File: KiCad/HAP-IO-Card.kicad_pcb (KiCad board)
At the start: 2 copper layers, 110 x 72 mm, 369 parts, among them CON601 AVR-JTAG-10, J201 TE_Connectivity_1-282834-0, J202 TE_Connectivity_282834-6, J203 GS3, J204 GS3, J205 GS3, J206 GS3, J207 GS3, J208 GS3, J209 GS3, J210 GS3, J211 TE_Connectivity_282834-6, J212 TE_Connectivity_1-282834-0, J401 TE_Connectivity_1-282834-0, J402 TE_Connectivity_282834-6, J501 TE_Connectivity_282834-3, J502 CONN_01X03_FEMALE, J601 ISP0, J602 ISP1, J603 CONN_01X02, J604 CONN_01X02, J605 CONN_01X02, J606 CONN_01X02, J607 CONN_01X03, J608 CONN_01X03, J701 5V_I/O_2, J702 5V_I/O_1, J703 NEO1, J704 NEO2, J705 NEO3, J706 NEO4, J707 CONN_01X03, Q201 ZXTN25050DFHTA, Q202 ZXTN25050DFHTA, Q203 ZXTN25050DFHTA, Q204 ZXTN25050DFHTA, Q205 ZXTN25050DFHTA, Q206 ZXTN25050DFHTA, Q207 ZXTN25050DFHTA, Q208 ZXTN25050DFHTA, U201 LTV-354T, U202 LTV-354T, U203 LTV-354T, U204 LTV-354T, U205 LTV-354T, U206 LTV-354T, U207 LTV-354T, U208 LTV-354T, U209 MCP23017, U401 ADS1115IDGST, U402 ADS1115IDGST, U501 LM1086-5V, U502 LM1086-3.3V, U701 TXB0102DCT

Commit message: Groudplanes
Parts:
- removed the REF** at (38.4, 79.5)
- removed the REF** at (38.4, 76.9)
- removed the REF** at (38.4, 74.4)
- removed the REF** at (38.4, 71.8)
- removed the REF** at (38.4, 69.3)
- removed the REF** at (38.4, 66.8)
- removed the REF** at (38.4, 64.2)
- removed the REF** at (38.4, 61.7)
- removed the REF** at (38.4, 59.1)
- removed the REF** at (38.4, 56.6)
- removed the REF** at (38.4, 54.1)
- removed the REF** at (99.3, 61.6)
- removed the REF** at (97.5, 63.3)
- added REF**: StichingVia, StichingVIA:StichingVia, F.Cu at (77.0, 71.9)
- added REF**: StichingVia, StichingVIA:StichingVia, F.Cu at (93.0, 41.1)
- added REF**: StichingVia, StichingVIA:StichingVia, F.Cu at (48.0, 81.5)
- added REF**: StichingVia, StichingVIA:StichingVia, F.Cu at (49.5, 82.8)
- added REF**: StichingVia, StichingVIA:StichingVia, F.Cu at (52.3, 76.7)
- added REF**: StichingVia, StichingVIA:StichingVia, F.Cu at (54.6, 76.7)
- added REF**: StichingVia, StichingVIA:StichingVia, F.Cu at (54.6, 74.7)
- added REF**: StichingVia, StichingVIA:StichingVia, F.Cu at (93.2, 71.6)
- added REF**: StichingVia, StichingVIA:StichingVia, F.Cu at (55.9, 49.5)
- added REF**: StichingVia, StichingVIA:StichingVia, F.Cu at (53.3, 49.5)
- added REF**: StichingVia, StichingVIA:StichingVia, F.Cu at (50.8, 49.5)
- added REF**: StichingVia, StichingVIA:StichingVia, F.Cu at (78.7, 71.9)
- added REF**: StichingVia, StichingVIA:StichingVia, F.Cu at (48.2, 49.5)
- added REF**: StichingVia, StichingVIA:StichingVia, F.Cu at (45.7, 49.5)
- added REF**: StichingVia, StichingVIA:StichingVia, F.Cu at (73.5, 64.8)
- added REF**: StichingVia, StichingVIA:StichingVia, F.Cu at (73.5, 62.2)
- added REF**: StichingVia, StichingVIA:StichingVia, F.Cu at (86.1, 65.4)
- added REF**: StichingVia, StichingVIA:StichingVia, F.Cu at (92.3, 60.3)
- added REF**: StichingVia, StichingVIA:StichingVia, F.Cu at (92.3, 62.9)
- added REF**: StichingVia, StichingVIA:StichingVia, F.Cu at (87.1, 67.7)
- added REF**: StichingVia, StichingVIA:StichingVia, F.Cu at (88.7, 60.4)
- added REF**: StichingVia, StichingVIA:StichingVia, F.Cu at (88.7, 65.4)
- added REF**: StichingVia, StichingVIA:StichingVia, F.Cu at (81.0, 71.9)
- added REF**: StichingVia, StichingVIA:StichingVia, F.Cu at (88.7, 62.9)
- added REF**: StichingVia, StichingVIA:StichingVia, F.Cu at (62.6, 70.0)
- added REF**: StichingVia, StichingVIA:StichingVia, F.Cu at (62.6, 62.4)
- added REF**: StichingVia, StichingVIA:StichingVia, F.Cu at (62.6, 67.5)
- added REF**: StichingVia, StichingVIA:StichingVia, F.Cu at (62.6, 64.9)
- added REF**: StichingVia, StichingVIA:StichingVia, F.Cu at (59.0, 62.4)
- added REF**: StichingVia, StichingVIA:StichingVia, F.Cu at (59.0, 70.0)
- added REF**: StichingVia, StichingVIA:StichingVia, F.Cu at (59.0, 64.9)
- added REF**: StichingVia, StichingVIA:StichingVia, F.Cu at (59.0, 67.5)
- added REF**: StichingVia, StichingVIA:StichingVia, F.Cu at (50.2, 64.9)
- added REF**: StichingVia, StichingVIA:StichingVia, F.Cu at (83.8, 71.9)
- added REF**: StichingVia, StichingVIA:StichingVia, F.Cu at (50.2, 67.4)
- added REF**: StichingVia, StichingVIA:StichingVia, F.Cu at (50.2, 70.0)
- added REF**: StichingVia, StichingVIA:StichingVia, F.Cu at (50.2, 62.4)
- added REF**: StichingVia, StichingVIA:StichingVia, F.Cu at (53.1, 62.4)
- added REF**: StichingVia, StichingVIA:StichingVia, F.Cu at (53.1, 70.0)
- added REF**: StichingVia, StichingVIA:StichingVia, F.Cu at (53.1, 67.4)
- added REF**: StichingVia, StichingVIA:StichingVia, F.Cu at (53.1, 64.9)
- added REF**: StichingVia, StichingVIA:StichingVia, F.Cu at (46.6, 70.0)
- added REF**: StichingVia, StichingVIA:StichingVia, F.Cu at (46.6, 67.4)
- added REF**: StichingVia, StichingVIA:StichingVia, F.Cu at (46.6, 64.9)
- added REF**: StichingVia, StichingVIA:StichingVia, F.Cu at (88.6, 82.3)
- added REF**: StichingVia, StichingVIA:StichingVia, F.Cu at (46.6, 62.4)
- added REF**: StichingVia, StichingVIA:StichingVia, F.Cu at (87.1, 83.3)
- added REF**: StichingVia, StichingVIA:StichingVia, F.Cu at (87.1, 81.8)
- added REF**: StichingVia, StichingVIA:StichingVia, F.Cu at (49.5, 81.5)
- added REF**: StichingVia, StichingVIA:StichingVia, F.Cu at (99.6, 42.7)
- moved REF** 0.88 mm to (99.8, 65.3)
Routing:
- net DIGITAL_INTA: track 63.5 -> 62.9 mm
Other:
- board text added: "1"
- board text added: "5VI/O1"
- board text added: "5VI/O2"
- board text added: "I38"
- board text added: "I39"
- board text added: "IO0/ Btn"
- board text added: "IO5/ LED"
- board text added: "JTAG"

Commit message: More groundplane
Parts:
- added REF**: StichingVia, StichingVIA:StichingVia, F.Cu at (117.1, 63.2)
- added REF**: StichingVia, StichingVIA:StichingVia, F.Cu at (119.1, 61.2)
- added REF**: StichingVia, StichingVIA:StichingVia, F.Cu at (126.2, 45.5)
- added REF**: StichingVia, StichingVIA:StichingVia, F.Cu at (126.2, 61.2)
- added REF**: StichingVia, StichingVIA:StichingVia, F.Cu at (126.2, 71.4)
- added REF**: StichingVia, StichingVIA:StichingVia, F.Cu at (132.1, 71.4)
- added REF**: StichingVia, StichingVIA:StichingVia, F.Cu at (121.7, 71.6)
- added REF**: StichingVia, StichingVIA:StichingVia, F.Cu at (118.1, 69.1)
- added REF**: StichingVia, StichingVIA:StichingVia, F.Cu at (114.3, 67.1)
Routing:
- net Earth: track 95.2 -> 83.7 mm, vias 16 -> 15
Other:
- net class 12V: trace_width 0.4 -> 1.27
- net class 3V3: trace_width 0.3 -> 0.76
- net class 5V: trace_width 0.3 -> 0.76
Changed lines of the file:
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@@
 (kicad_pcb (version 20170123) (host pcbnew "(2017-05-31 revision c0bb8a30c)-makepkg")
   (general
-    (links 649)
+    (links 660)
     (no_connects 0)
     (area 34.499762 15.011666 148.383572 90.7625)
     (thickness 1.6)
     (drawings 198)
-    (tracks 1824)
+    (tracks 1818)
     (zones 0)
-    (modules 406)
+    (modules 415)
     (nets 162)
   )
@@
   (net_class 12V ""
     (clearance 0.3)
-    (trace_width 0.4)
+    (trace_width 1.27)
     (via_dia 0.6)
     (via_drill 0.4)
@@
   (net_class 3V3 ""
     (clearance 0.2)
-    (trace_width 0.3)
+    (trace_width 0.76)
     (via_dia 0.6)
     (via_drill 0.4)
@@
   (net_class 5V ""
     (clearance 0.2)
-    (trace_width 0.3)
+    (trace_width 0.76)
     (via_dia 0.6)
     (via_drill 0.4)
@@
   )
   (module StichingVIA:StichingVia locked (layer F.Cu)
+    (at 117.094 63.246)
+    (fp_text reference REF** (at -0.65 0.03) (layer F.SilkS) hide
+      (effects (font (size 0.127 0.127) (thickness 0.03175)))
+    )
+    (fp_text value StichingVia (at -0.86 0.14) (layer F.Fab) hide
+      (effects (font (size 0.127 0.127) (thickness 0.03175)))
+    )
+    (fp_circle (center 0 0) (end 0.22 0.12) (layer F.CrtYd) (width 0.1))
+    (fp_circle (center 0 0) (end 0.25 0) (layer B.CrtYd) (width 0.1))
+    (pad 1 thru_hole circle (at 0 0) (size 0.6 0.6) (drill 0.3) (layers *.Cu)
+      (net 94 Earth) (zone_connect 2))
+  )
+  (module StichingVIA:StichingVia locked (layer F.Cu)
+    (at 119.126 61.214)
+    (fp_text reference REF** (at -0.65 0.03) (layer F.SilkS) hide
+      (effects (font (size 0.127 0.127) (thickness 0.03175)))
+    )
+    (fp_text value StichingVia (at -0.86 0.14) (layer F.Fab) hide
+      (effects (font (size 0.127 0.127) (thickness 0.03175)))
+    )
+    (fp_circle (center 0 0) (end 0.25 0) (layer B.CrtYd) (width 0.1))
+    (fp_circle (center 0 0) (end 0.22 0.12) (layer F.CrtYd) (width 0.1))
+    (pad 1 thru_hole circle (at 0 0) (size 0.6 0.6) (drill 0.3) (layers *.Cu)
+      (net 94 Earth) (zone_connect 2))
+  )
+  (module StichingVIA:StichingVia locked (layer F.Cu)
+    (at 126.238 45.466)
+    (fp_text reference REF** (at -0.65 0.03) (layer F.SilkS) hide
+      (effects (font (size 0.127 0.127) (thickness 0.03175)))
+    )
+    (fp_text value StichingVia (at -0.86 0.14) (layer F.Fab) hide
+      (effects (font (size 0.127 0.127) (thickness 0.03175)))
+    )
+    (fp_circle (center 0 0) (end 0.25 0) (layer B.CrtYd) (width 0.1))
+    (fp_circle (center 0 0) (end 0.22 0.12) (layer F.CrtYd) (width 0.1))
+    (pad 1 thru_hole circle (at 0 0) (size 0.6 0.6) (drill 0.3) (layers *.Cu)
+      (net 94 Earth) (zone_connect 2))
+  )
+  (module StichingVIA:StichingVia locked (layer F.Cu)
+    (at 126.238 61.214)
+    (fp_text reference REF** (at -0.65 0.03) (layer F.SilkS) hide
+      (effects (font (size 0.127 0.127) (thickness 0.03175)))
+    )
+    (fp_text value StichingVia (at -0.86 0.14) (layer F.Fab) hide
+      (effects (font (size 0.127 0.127) (thickness 0.03175)))
+    )
+    (fp_circle (center 0 0) (end 0.22 0.12) (layer F.CrtYd) (width 0.1))
+    (fp_circle (center 0 0) (end 0.25 0) (layer B.CrtYd) (width 0.1))
+    (pad 1 thru_hole circle (at 0 0) (size 0.6 0.6) (drill 0.3) (layers *.Cu)
+      (net 94 Earth) (zone_connect 2))
+  )
+  (module StichingVIA:StichingVia locked (layer F.Cu)
+    (at 126.238 71.374)
+    (fp_text reference REF** (at -0.65 0.03) (layer F.SilkS) hide
+      (effects (font (size 0.127 0.127) (thickness 0.03175)))
+    )
+    (fp_text value StichingVia (at -0.86 0.14) (layer F.Fab) hide
+      (effects (font (size 0.127 0.127) (thickness 0.03175)))
+    )
+    (fp_circle (center 0 0) (end 0.25 0) (layer B.CrtYd) (width 0.1))
+    (fp_circle (center 0 0) (end 0.22 0.12) (layer F.CrtYd) (width 0.1))
+    (pad 1 thru_hole circle (at 0 0) (size 0.6 0.6) (drill 0.3) (layers *.Cu)
+      (net 94 Earth) (zone_connect 2))
+  )
+  (module StichingVIA:StichingVia locked (layer F.Cu)
+    (at 132.08 71.374)
+    (fp_text reference REF** (at -0.65 0.03) (layer F.SilkS) hide
+      (effects (font (size 0.127 0.127) (thickness 0.03175)))
+    )
+    (fp_text value StichingVia (at -0.86 0.14) (layer F.Fab) hide
+      (effects (font (size 0.127 0.127) (thickness 0.03175)))
+    )
+    (fp_circle (center 0 0) (end 0.25 0) (layer B.CrtYd) (width 0.1))
+    (fp_circle (center 0 0) (end 0.22 0.12) (layer F.CrtYd) (width 0.1))
+    (pad 1 thru_hole circle (at 0 0) (size 0.6 0.6) (drill 0.3) (layers *.Cu)
+      (net 94 Earth) (zone_connect 2))
+  )
+  (module StichingVIA:StichingVia locked (layer F.Cu)
+    (at 121.666 71.628)
+    (fp_text reference REF** (at -0.65 0.03) (layer F.SilkS) hide
+      (effects (font (size 0.127 0.127) (thickness 0.03175)))
+    )
+    (fp_text value StichingVia (at -0.86 0.14) (layer F.Fab) hide
+      (effects (font (size 0.127 0.127) (thickness 0.03175)))
+    )
+    (fp_circle (center 0 0) (end 0.22 0.12) (layer F.CrtYd) (width 0.1))
+    (fp_circle (center 0 0) (end 0.25 0) (layer B.CrtYd) (width 0.1))
+    (pad 1 thru_hole circle (at 0 0) (size 0.6 0.6) (drill 0.3) (layers *.Cu)
+      (net 94 Earth) (zone_connect 2))
+  )
+  (module StichingVIA:StichingVia locked (layer F.Cu)
+    (at 118.11 69.088)
+    (fp_text reference REF** (at -0.65 0.03) (layer F.SilkS) hide
+      (effects (font (size 0.127 0.127) (thickness 0.03175)))
+    )
+    (fp_text value StichingVia (at -0.86 0.14) (layer F.Fab) hide
+      (effects (font (size 0.127 0.127) (thickness 0.03175)))
+    )
+    (fp_circle (center 0 0) (end 0.25 0) (layer B.CrtYd) (width 0.1))
+    (fp_circle (center 0 0) (end 0.22 0.12) (layer F.CrtYd) (width 0.1))
+    (pad 1 thru_hole circle (at 0 0) (size 0.6 0.6) (drill 0.3) (layers *.Cu)
+      (net 94 Earth) (zone_connect 2))
+  )
+  (module StichingVIA:StichingVia locked (layer F.Cu)
+    (at 114.3 67.056)
+    (fp_text reference REF** (at -0.65 0.03) (layer F.SilkS) hide
+      (effects (font (size 0.127 0.127) (thickness 0.03175)))
+    )
+    (fp_text value StichingVia (at -0.86 0.14) (layer F.Fab) hide
+      (effects (font (size 0.127 0.127) (thickness 0.03175)))
+    )
+    (fp_circle (center 0 0) (end 0.22 0.12) (layer F.CrtYd) (width 0.1))
+    (fp_circle (center 0 0) (end 0.25 0) (layer B.CrtYd) (width 0.1))
+    (pad 1 thru_hole circle (at 0 0) (size 0.6 0.6) (drill 0.3) (layers *.Cu)
+      (net 94 Earth) (zone_connect 2))
+  )
+  (module StichingVIA:StichingVia locked (layer F.Cu)
     (at 76.962 71.882)
     (fp_text reference REF** (at -0.65 0.03) (layer F.SilkS) hide
@@
   (segment (start 108.88 28.72) (end 108.88 28.88) (width 0.25) (layer F.Cu) (net 94) (status 30))
   (segment (start 103.83 28.72) (end 103.92 28.72) (width 0.25) (layer F.Cu) (net 94) (status 30))
-  (segment (start 126.4 72.2) (end 129.96 72.2) (width 0.25) (layer B.Cu) (net 94) (status 20))
   (segment (start 129.96 72.2) (end 130.23 72.47) (width 0.25) (layer B.Cu) (net 94) (status 30))
-  (segment (start 132 76.4) (end 129.245001 73.645001) (width 0.25) (layer F.Cu) (net 94))
-  (segment (start 129.245001 73.645001) (end 126.844999 73.645001) (width 0.25) (layer F.Cu) (net 94))
-  (segment (start 126.844999 73.645001) (end 126.4 73.200002) (width 0.25) (layer F.Cu) (net 94))
-  (segment (start 126.4 73.200002) (end 126.4 72.2) (width 0.25) (layer F.Cu) (net 94))
-  (via (at 126.4 72.2) (size 0.6) (drill 0.4) (layers F.Cu B.Cu) (net 94))
   (segment (start 130.23 77.72) (end 130.68 77.72) (width 0.25) (layer B.Cu) (net 94) (status 30))
   (segment (start 130.68 77.72) (end 132 76.4) (width 0.25) (layer B.Cu) (net 94) (status 10))

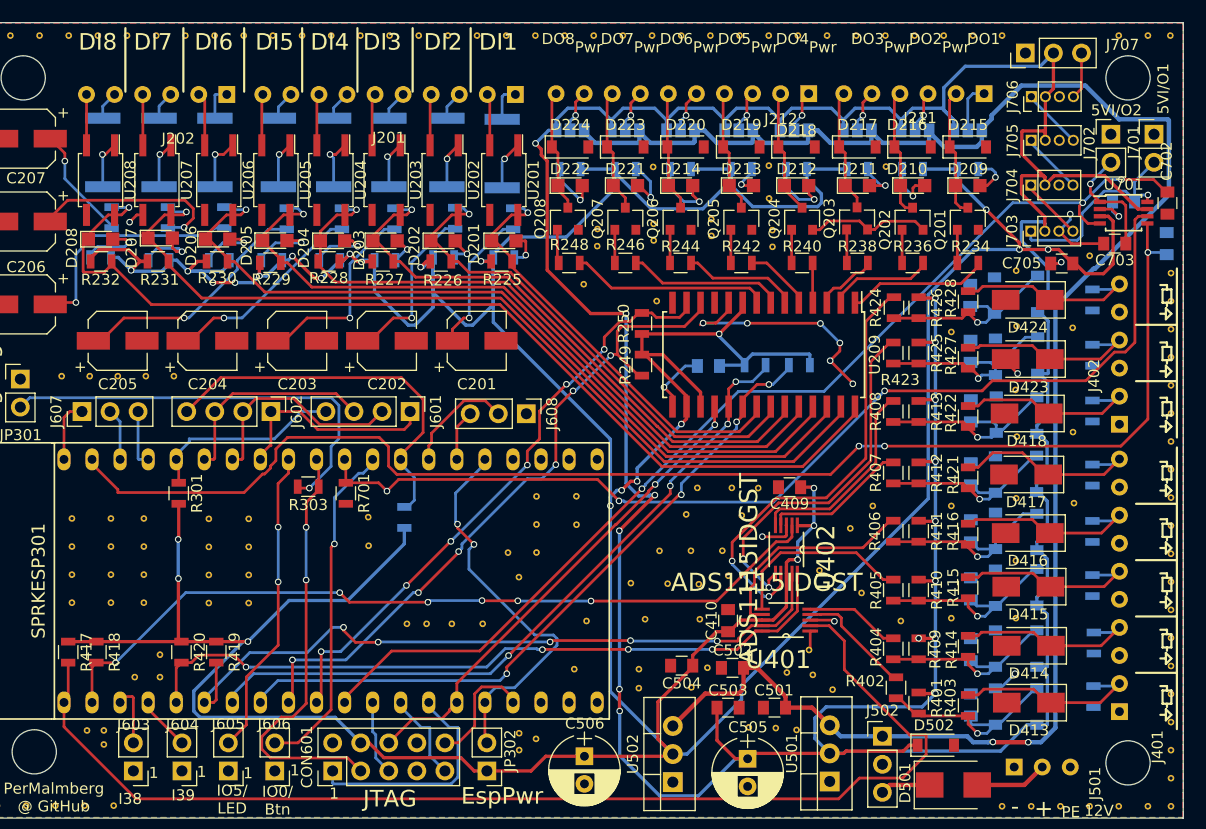
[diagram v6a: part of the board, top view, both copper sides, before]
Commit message: Increased width of 12V rail
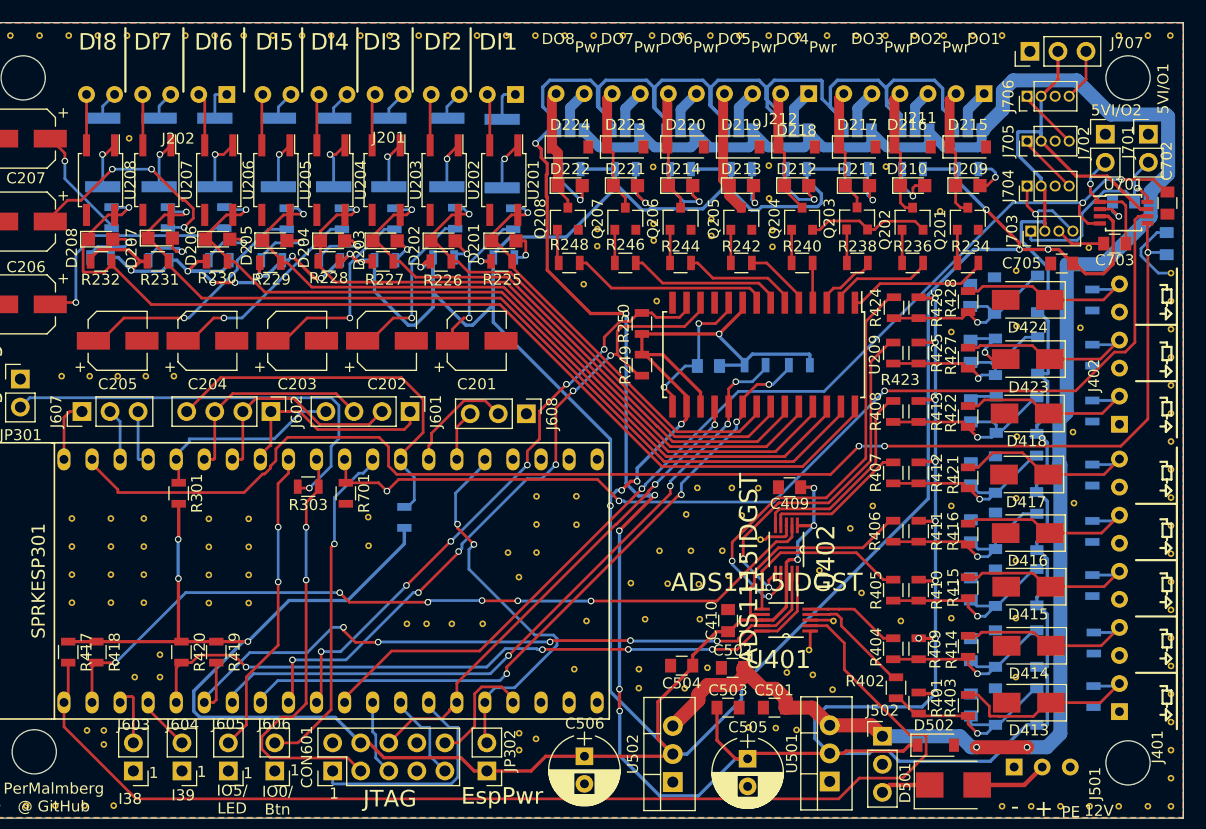
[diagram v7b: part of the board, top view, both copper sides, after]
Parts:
- removed the REF** at (132.1, 50.7)
- added REF**: StichingVia, StichingVIA:StichingVia, F.Cu at (51.8, 27.9)
- added REF**: StichingVia, StichingVIA:StichingVia, F.Cu at (115.6, 71.6)
- added REF**: StichingVia, StichingVIA:StichingVia, F.Cu at (132.1, 76.7)
- added REF**: StichingVia, StichingVIA:StichingVia, F.Cu at (109.0, 64.3)
- added REF**: StichingVia, StichingVIA:StichingVia, F.Cu at (125.2, 34.5)
- moved REF** 0.73 mm to (138.7, 37.8)
- moved REF** 0.70 mm to (137.9, 45.1)
- moved REF** 0.61 mm to (102.1, 77.7)
- moved J701 0.51 mm to (144.1, 27.6)
- moved J702 0.51 mm to (140.2, 27.6)
- moved J707 0.44 mm to (133.3, 20.1)
- moved J706 0.39 mm to (133.1, 24.1)
- moved J705 0.38 mm to (133.1, 28.2)
- moved J704 0.36 mm to (133.1, 32.3)
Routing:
- net POWER5V: track 346.2 -> 377.1 mm
- net +12V: track 168.9 -> 175.6 mm
- net Earth: track 83.7 -> 77.4 mm, vias 15 -> 4
- net Net-(C207-Pad1): track 17.8 -> 20.1 mm, vias 1 -> 3
- net Net-(D213-Pad2): track 2.93 -> 4.79 mm
- net Net-(J703-Pad4): track 5.74 -> 7.49 mm, vias 0 -> 1
- net /Digital I/O/PWR_DO_4: track 3.87 -> 5.34 mm, vias 1 -> 0
- net /Digital I/O/PWR_DO_5: track 3.84 -> 5.19 mm, vias 1 -> 0
- net POWER3V3: track 469.6 -> 470.8 mm
- net /Digital I/O/PWR_DO_2: track 3.81 -> 4.95 mm, vias 1 -> 0
- net /Sense Inputs/Sense1_DUT: track 17.6 -> 18.7 mm
- net Net-(C704-Pad1): track 20.0 -> 20.7 mm
- net Net-(D211-Pad2): track 3.83 -> 4.42 mm
- net /Digital I/O/PWR_DO_1: track 4.53 -> 3.94 mm
- net /Digital I/O/PWR_DO_6: vias 1 -> 0
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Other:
- net class 3V3: trace_width 0.76 -> 0.3
- net class 5V: trace_width 0.76 -> 0.3
